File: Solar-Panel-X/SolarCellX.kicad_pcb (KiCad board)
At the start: 6 copper layers, 48.4 x 48.4 mm, 62 parts, among them J1 XF2M-1015-1A, U2 Value, U3 TSL2561

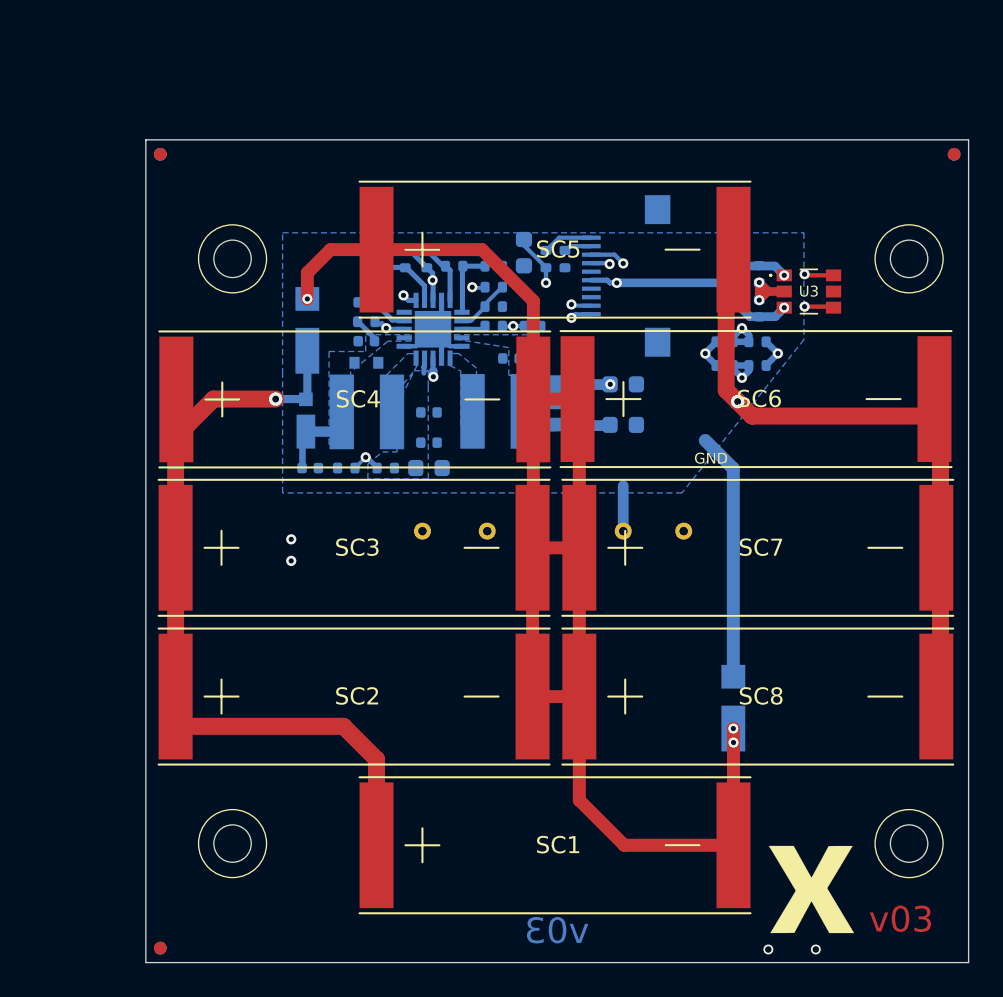
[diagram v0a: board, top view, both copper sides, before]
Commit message: Moved board connectors to North board edges
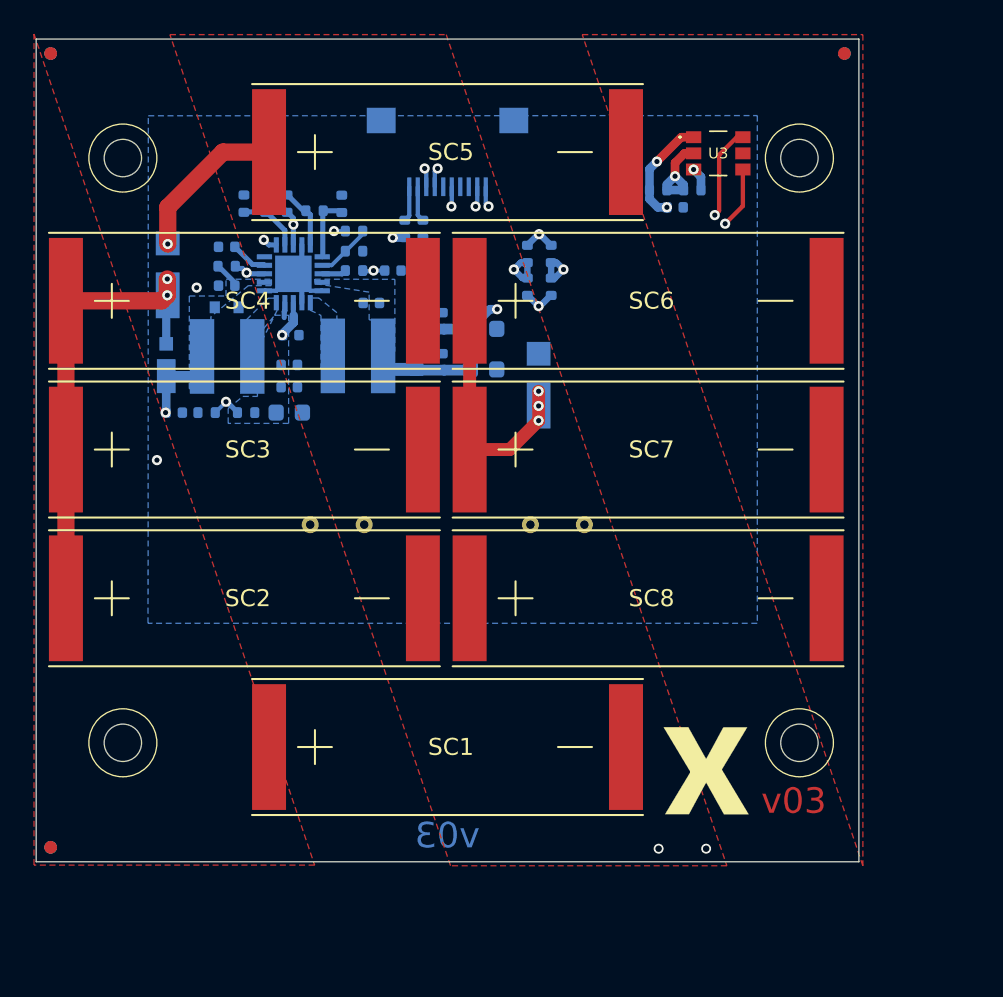
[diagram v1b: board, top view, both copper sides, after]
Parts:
- added Ref**: Val**, custom-footprints:pycubed_mini_logo, B.Cu at (129.9, 111.1)
- C6: footprint Capacitor_SMD:C_0603_1608Metric -> Capacitor_SMD:C_0402_1005Metric
- moved D5 22.2 mm to (143.9, 89.0)
- moved C6 14.5 mm to (129.3, 86.0), turned to 0 degrees
- moved R4 14.5 mm to (143.2, 81.2), turned to 90 degrees
- moved R2 13.8 mm to (144.6, 81.2), turned to 90 degrees
- moved R19 12.1 mm to (143.2, 83.2), turned to 90 degrees
- moved R3 11.2 mm to (144.6, 83.2), turned to 90 degrees
- moved J1 9.95 mm to (138.5, 77.3), turned to 0 degrees
- moved U3 9.72 mm to (154.4, 75.3)
- moved R9 9.66 mm to (132.3, 78.3), turned to -90 degrees
- moved REF** 9.34 mm to (153.7, 113.1)
- moved R10 8.86 mm to (133.0, 79.9)
- moved D3 8.84 mm to (122.0, 87.8)
- moved R6 8.84 mm to (126.5, 78.3)
- moved C1 8.84 mm to (135.3, 82.2)
- moved C10 8.84 mm to (138.2, 87.6)
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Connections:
- TP4 pad 1: /VSOLAR_FULL -> VSOLAR
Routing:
- net Net-(D4-Pad2): track 89.5 -> 24.7 mm, vias 3 -> 4
- net GND: track 69.3 -> 10.1 mm, vias 2 -> 1
- net /coil: track 12873.0 -> 12835.3 mm
- net /VSOLAR_FULL: track 58.0 -> 27.4 mm, vias 1 -> 2
- net +3V3: track 32.4 -> 50.9 mm, vias 3 -> 4
- net VSOLAR: track 5.68 -> 18.0 mm, vias 0 -> 1
- net SDA1: track 15.1 -> 25.8 mm
- net SCL1: track 15.8 -> 23.6 mm
- net COIL_P: track 16.6 -> 10.4 mm
- net COIL_N: track 14.8 -> 8.72 mm
- net Net-(R12-Pad1): track 3.47 -> 5.13 mm, vias 2 -> 1
- net BATT_P: track 2.99 -> 2.08 mm
- net VBAT: track 27.5 -> 28.1 mm
- added copper zone on F.Cu, net /VSOLAR_FULL
- added copper zone on F.Cu, net GND
- added copper zone on F.Cu, net Net-(D4-Pad2)
- removed copper zone on In3.Cu, net GND

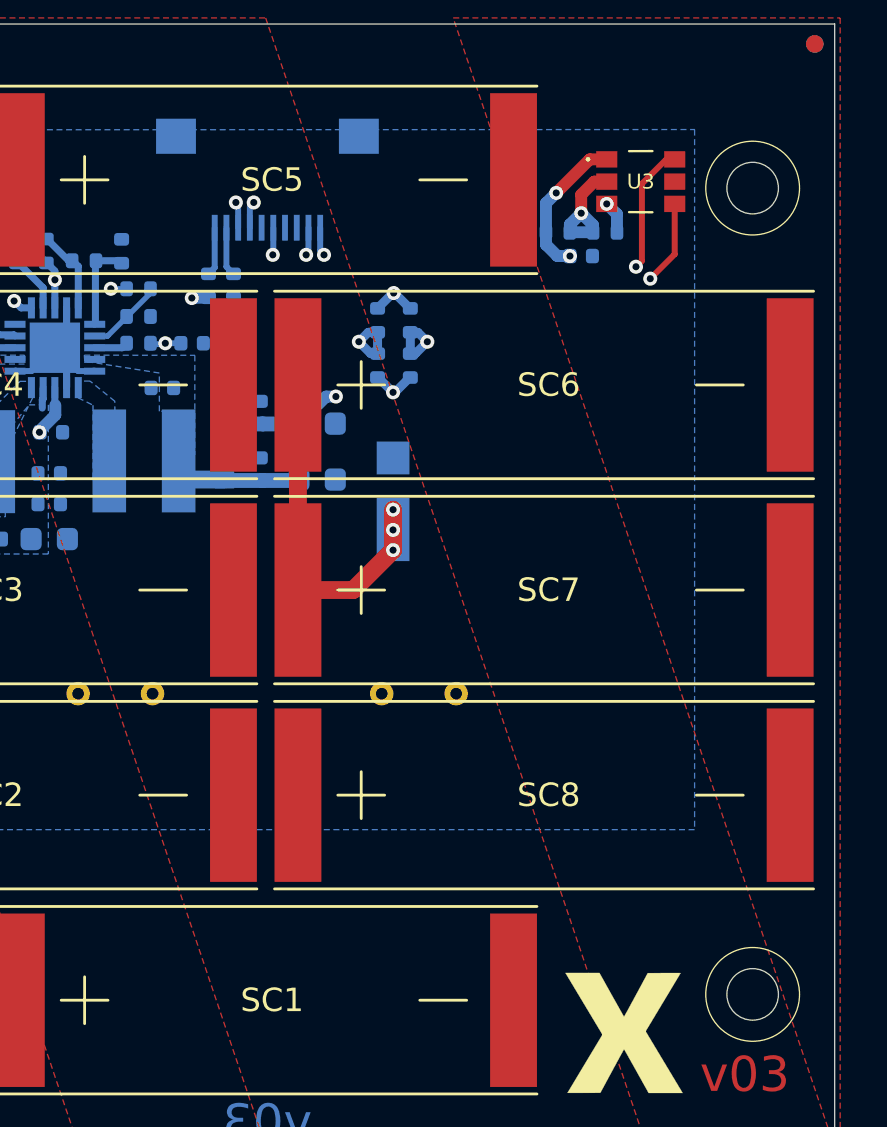
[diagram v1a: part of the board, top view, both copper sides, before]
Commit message: Added JLC order number silkscreen
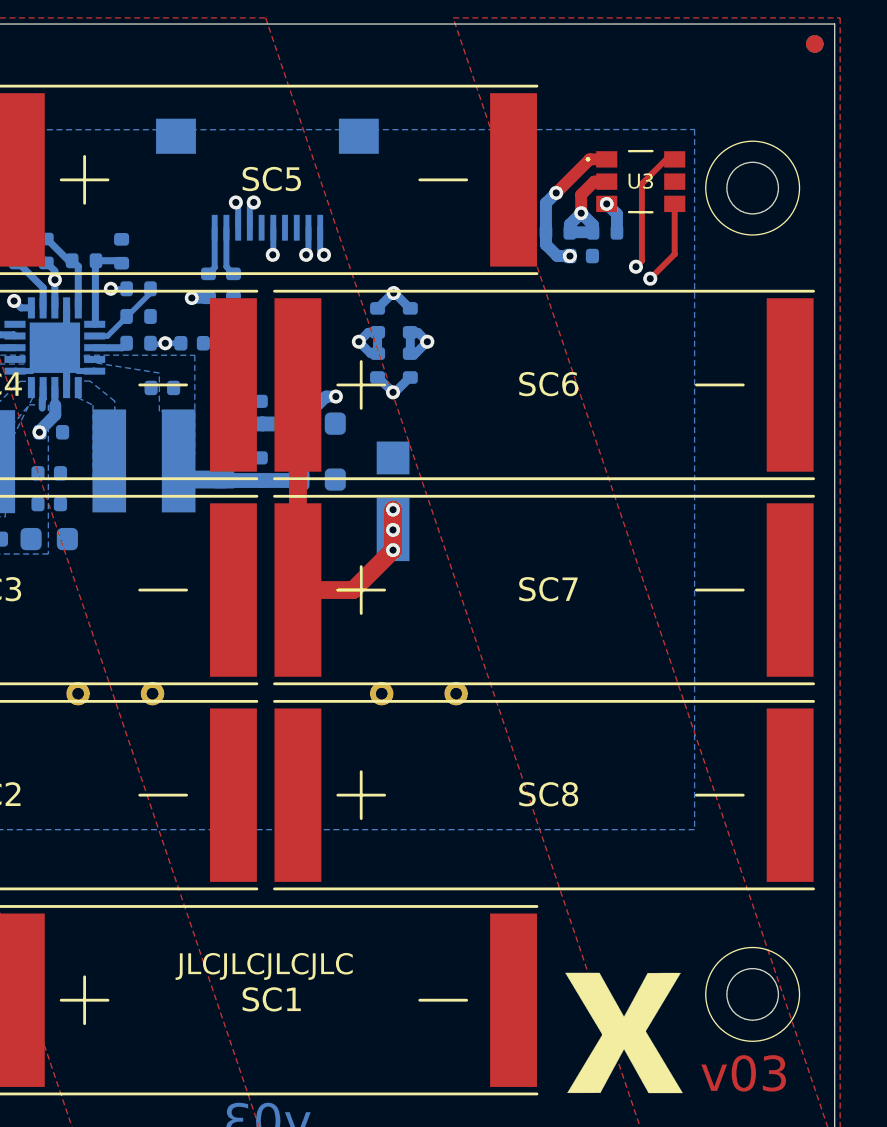
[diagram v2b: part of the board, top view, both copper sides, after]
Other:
- board text added: "JLCJLCJLCJLC"
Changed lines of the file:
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@@
   (gr_line (start 143.8656 83.82635) (end 143.8656 83.50885) (layer "B.SilkS") (width 0.12))
   (gr_circle (center 119.40699 75.58699) (end 121.40699 75.58699) (layer "F.SilkS") (width 0.05) (fill none))
-  (gr_circle (center 159.20699 75.58699) (end 161.20699 75.58699) (layer "F.SilkS") (width 0.05) (fill none))
+  (gr_circle (center 159.206997 75.586996) (end 161.206997 75.586996) (layer "F.SilkS") (width 0.05) (fill none))
   (gr_circle (center 159.20699 109.98699) (end 161.20699 109.98699) (layer "F.SilkS") (width 0.05) (fill none))
   (gr_circle (center 119.40699 109.98699) (end 121.40699 109.98699) (layer "F.SilkS") (width 0.05) (fill none))
@@
     (effects (font (size 0.762 0.762) (thickness 0.1016)) (justify left mirror))
   )
+  (gr_text "JLCJLCJLCJLC" (at 138.43 108.712) (layer "F.SilkS")
+    (effects (font (size 0.889 0.889) (thickness 0.15)))
+  )
   (gr_text "v03\n" (at 138.4935 115.443) (layer "B.Mask")

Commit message: Made Requested Changes
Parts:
- moved TP2 45.9 mm to (111.4, 64.1)
- moved TP3 45.9 mm to (101.7, 64.1)
- moved TP4 45.9 mm to (98.5, 64.1)
- moved TP1 45.9 mm to (114.6, 64.1)
- moved R3 43.5 mm to (105.5, 64.1), turned to 0 degrees
- moved R19 42.9 mm to (105.5, 62.7), turned to 0 degrees
- moved D5 42.5 mm to (111.8, 61.1), turned to 180 degrees
- moved C5 41.8 mm to (115.6, 57.8), turned to 90 degrees
- moved SC2 41.4 mm to (84.0, 75.3)
- moved SC4 41.4 mm to (84.0, 57.8)
- moved SC3 41.4 mm to (84.0, 66.5)
- moved REF** 41.3 mm to (129.9, 43.2) (x2)
- moved REF** 41.3 mm to (121.8, 87.0)
- moved Ref** 41.3 mm to (97.9, 84.9)
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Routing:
- net Net-(D4-Pad2): track 24.7 -> 1.27 mm, vias 4 -> 3
- net +3V3: track 50.9 -> 33.4 mm, vias 4 -> 3
- net COIL_P: track 10.4 -> 23.2 mm
- net COIL_N: track 8.72 -> 20.9 mm
- net VBAT: track 28.1 -> 20.2 mm
- net Net-(R12-Pad1): track 5.13 -> 12.7 mm, vias 1 -> 2
- net SDA1: track 25.8 -> 18.6 mm
- net SCL1: track 23.6 -> 16.8 mm
- net VSOLAR: track 18.0 -> 11.5 mm
- net /coil: track 12835.3 -> 12829.8 mm
- net Net-(R10-Pad2): track 6.93 -> 10.3 mm
- net /VSOLAR_FULL: track 27.4 -> 24.4 mm, vias 2 -> 5
- net GND: track 10.1 -> 9.09 mm, vias 1 -> 3
- net BATT_N: track 2.09 -> 1.29 mm
- net BATT_P: track 2.08 -> 1.30 mm
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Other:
- rule pad_to_mask_clearance: 0.049 -> 0.0508

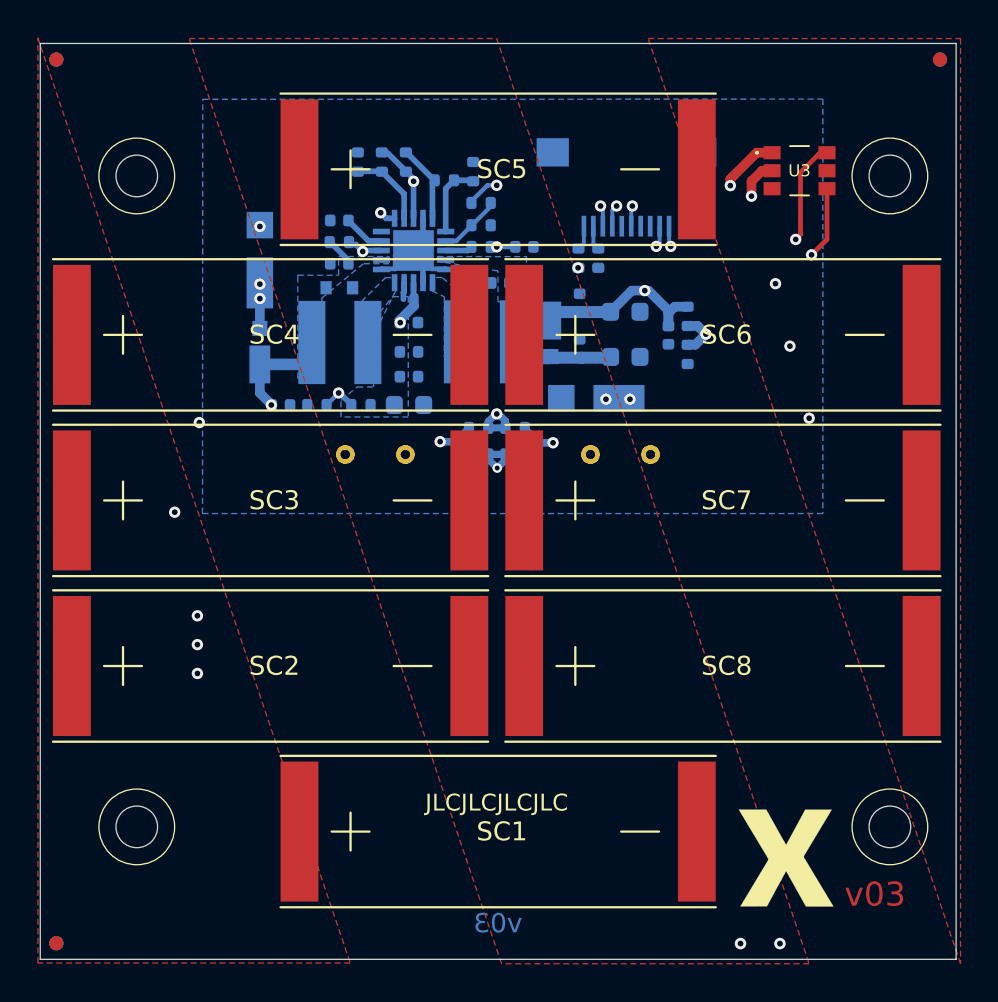
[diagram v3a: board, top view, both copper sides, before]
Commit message: Done with X, +/-Y, and +Z. TODO: -Z
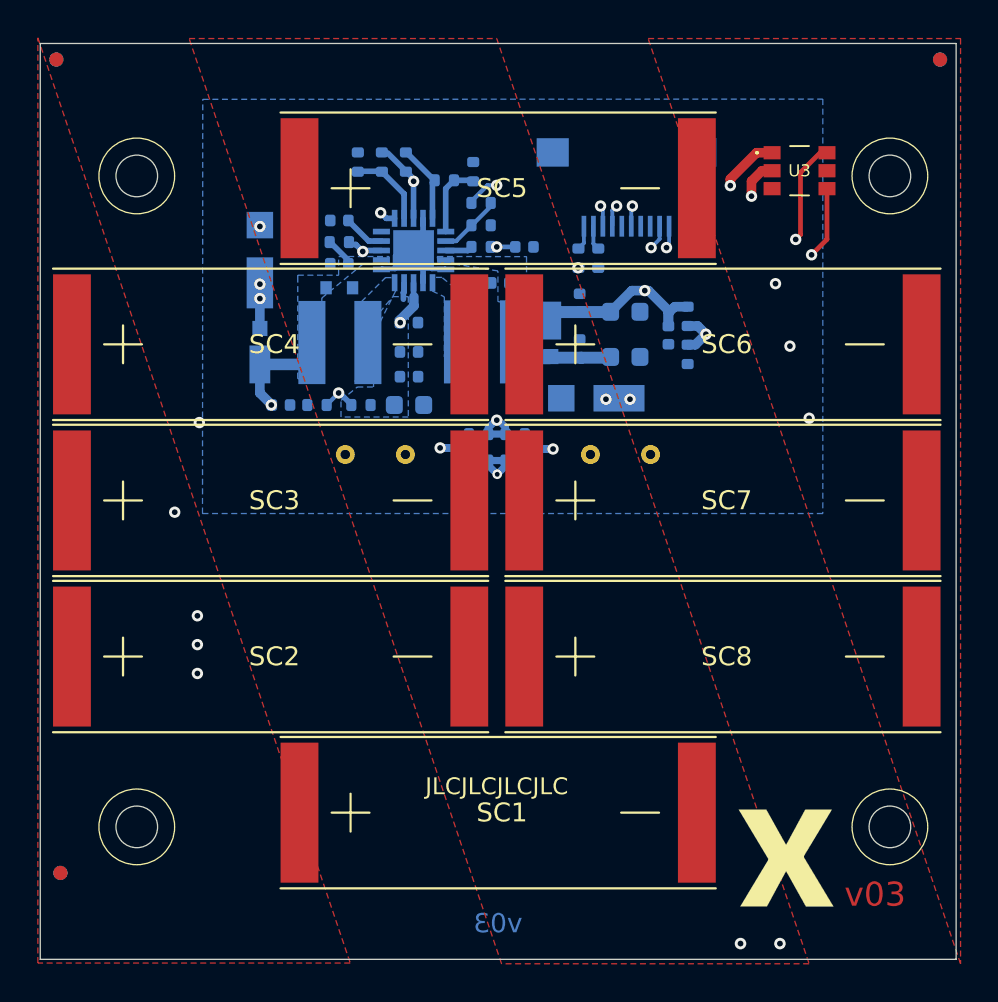
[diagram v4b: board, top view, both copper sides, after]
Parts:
- moved REF** 3.72 mm to (83.4, 86.2) (x2)
- moved SC1 1.00 mm to (96.1, 83.0)
- moved SC5 1.00 mm to (96.1, 50.0)
- moved SC2 0.50 mm to (84.0, 74.8)
- moved SC4 0.50 mm to (84.0, 58.3)
- moved SC6 0.50 mm to (108.0, 58.3)
- moved SC8 0.50 mm to (108.0, 74.8)
- moved R2 0.33 mm to (107.5, 64.4)
- moved R3 0.33 mm to (105.5, 64.4)
- moved R19 0.33 mm to (105.5, 63.0)
- moved R4 0.33 mm to (107.5, 63.0)
